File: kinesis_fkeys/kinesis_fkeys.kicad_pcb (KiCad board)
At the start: 2 copper layers, 123 x 60.5 mm, 40 parts, among them J1 RIGHT_13_TOP, J2 LEFT_13_TOP, J3 Conn_01x06, J4 Conn_01x06

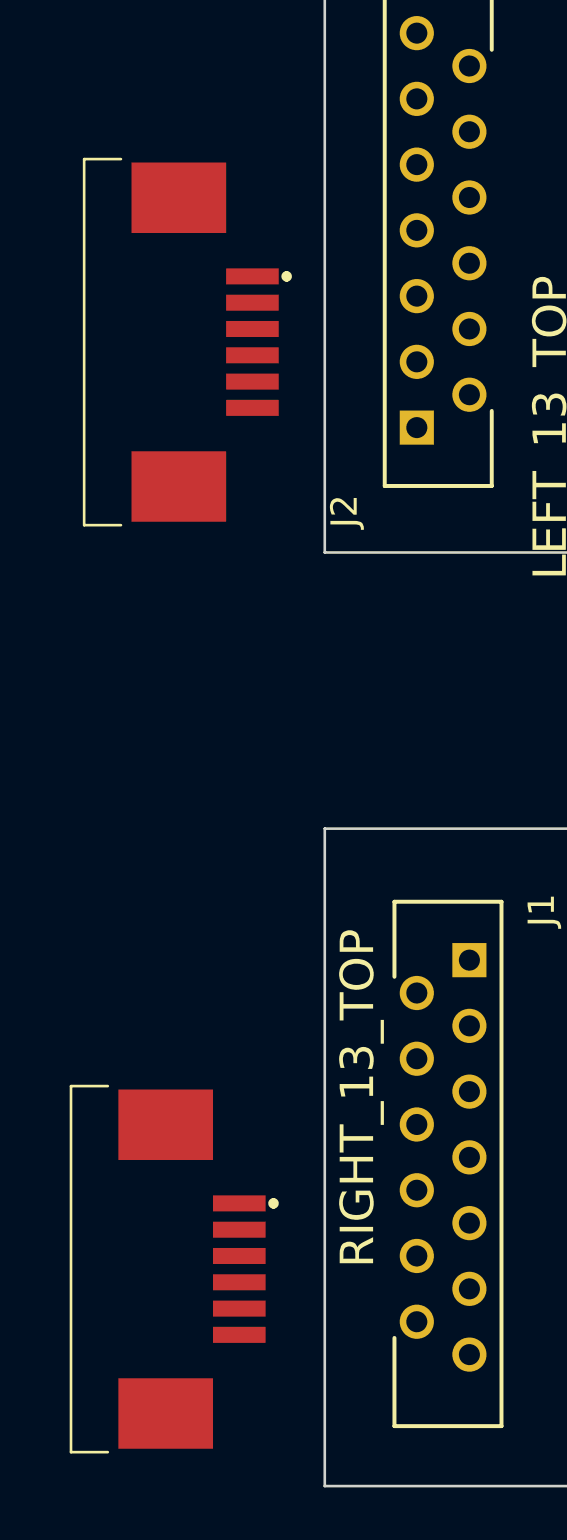
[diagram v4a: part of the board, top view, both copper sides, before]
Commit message: fixed wrong amount pins on the footprint and sorted pinout on the connectors
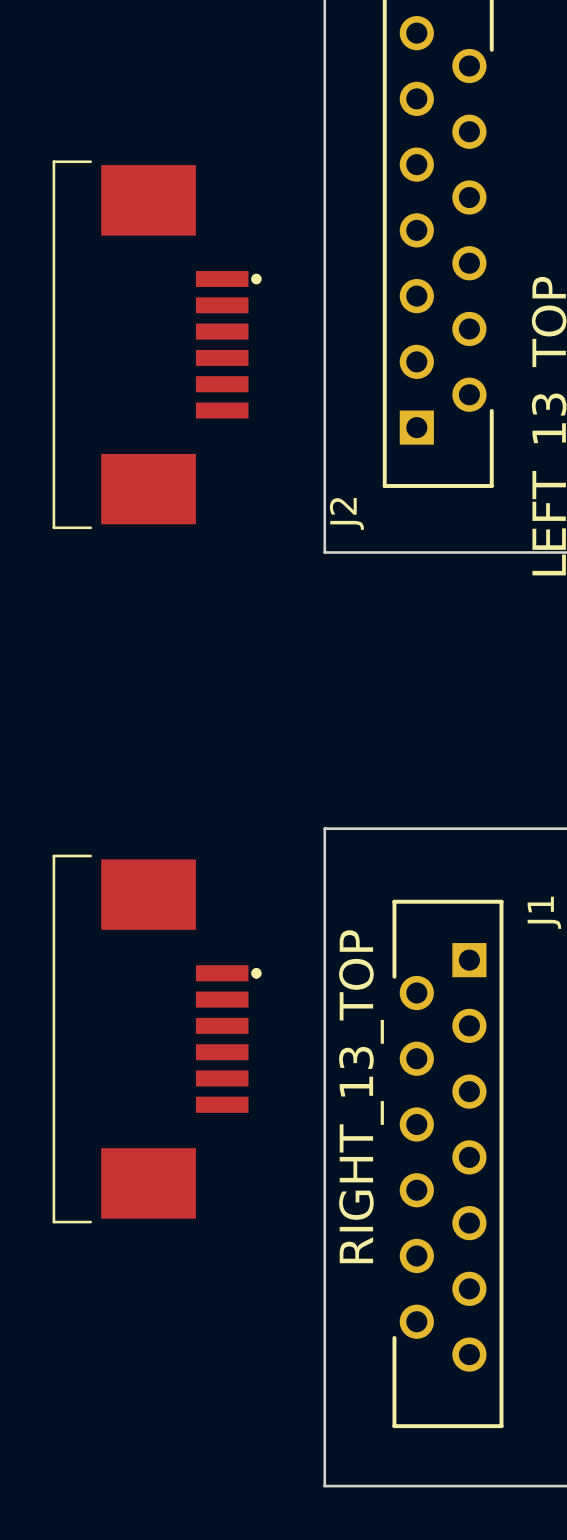
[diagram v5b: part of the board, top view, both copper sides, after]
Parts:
- removed J4: Conn_01x06, dodo_conn:84953-6
- added J5: Conn_01x08, dodo_conn:84953-6, F.Cu at (79.3, 80.2)
- J3: value Conn_01x06 -> Conn_01x08
- moved J3 8.77 mm to (79.3, 106.6)
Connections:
- J3 pad 1: /right_fkeys/COL_5 -> /right_fkeys/ROW_ESC
- J3 pad 2: /right_fkeys/COL_3 -> /right_fkeys/ROW_F1
- J3 pad 3: /right_fkeys/COL_4 -> /right_fkeys/ROW_F2
- J3 pad 4: /right_fkeys/ROW_F2 -> /right_fkeys/COL_3
- J3 pad 5: /right_fkeys/ROW_F1 -> /right_fkeys/COL_4
- J3 pad 6: /right_fkeys/ROW_ESC -> /right_fkeys/COL_5
- J3 pad 7: (no net) -> GND
- J3 pad 8: (no net) -> GND

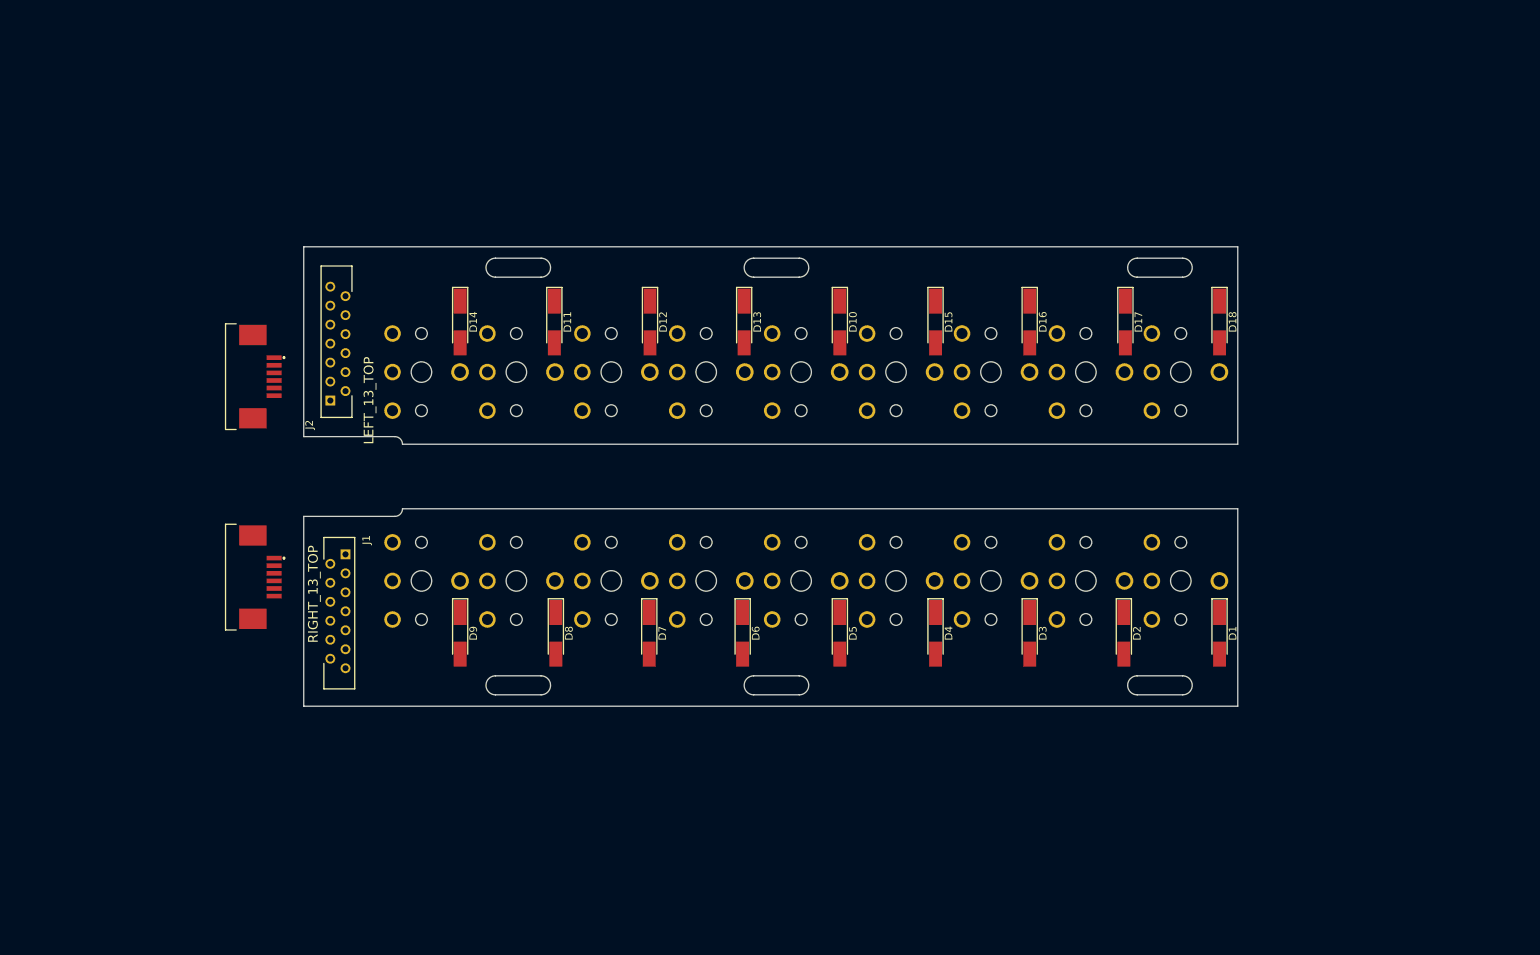
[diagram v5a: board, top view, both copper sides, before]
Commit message: positioning of components and added filled zones
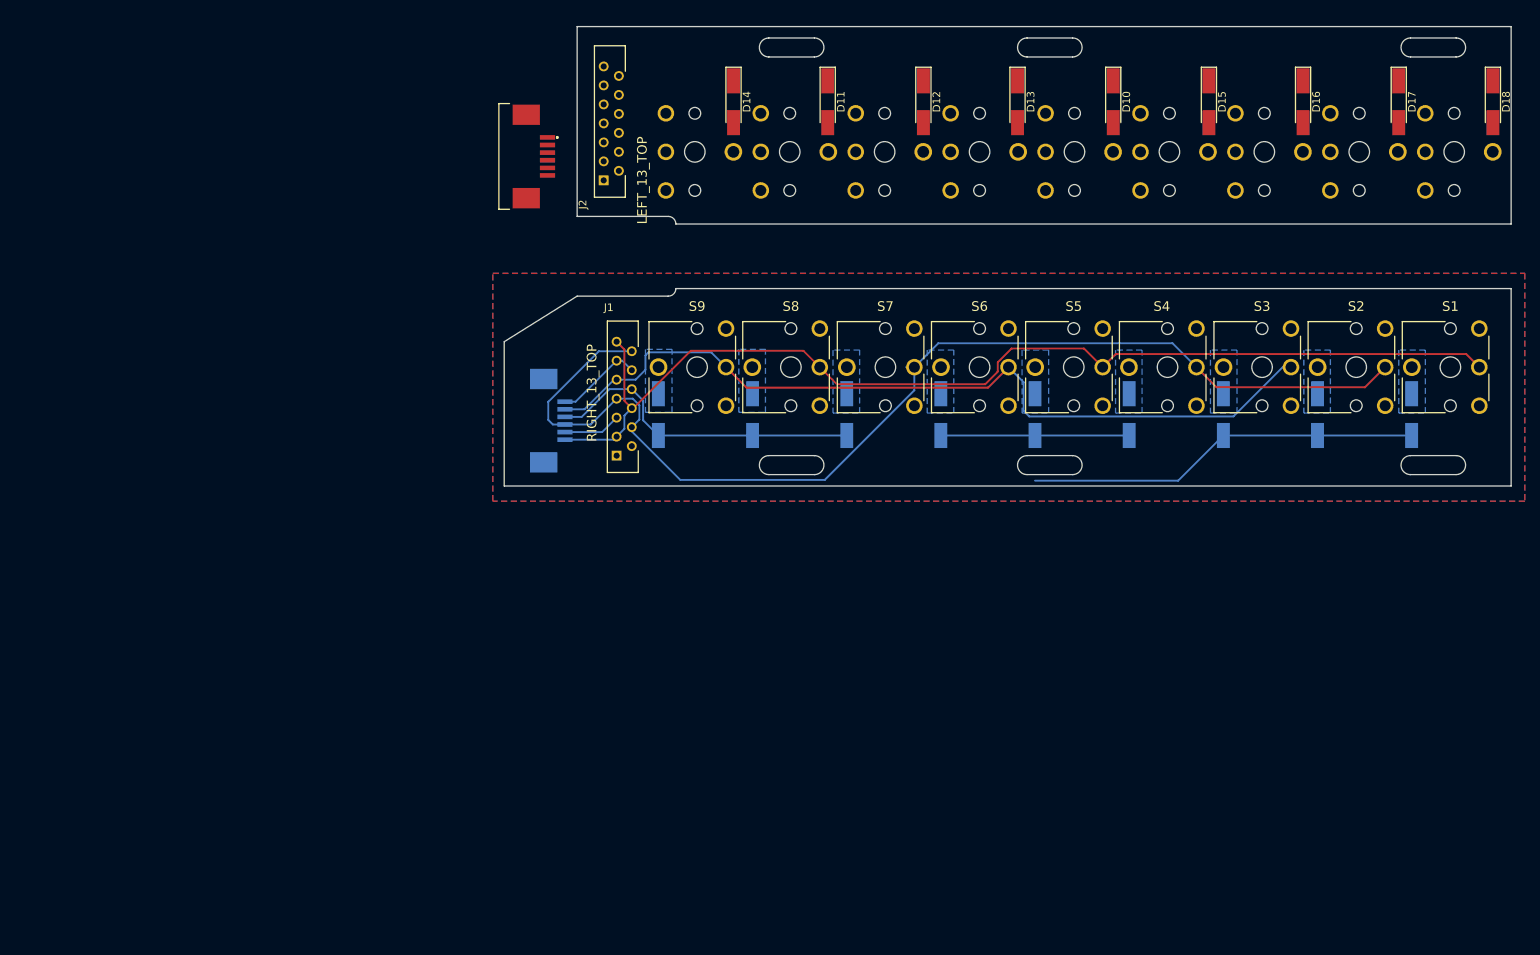
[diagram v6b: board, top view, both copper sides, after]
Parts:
- D1, D2, D3, D4, D5, D6, D7, D8, D9, J3: moved to B.Cu
- S1, S2, S3, S4, S5, S6, S7, S8, S9: moved to F.Cu
- moved S9 52.2 mm to (141.3, 73.9)
- moved S8 52.0 mm to (153.7, 73.9)
- moved S7 52.0 mm to (166.1, 73.9)
- moved S6 51.9 mm to (178.5, 73.9)
- moved S5 51.8 mm to (190.9, 73.9)
- moved S4 51.7 mm to (203.3, 73.9)
- moved S3 51.7 mm to (215.7, 73.9)
- moved S2 51.6 mm to (228.1, 73.9)
- moved S1 51.5 mm to (240.5, 73.9)
- moved S10 46.2 mm to (233.4, 45.5)
- moved S14 46.2 mm to (170.9, 45.5)
- moved S15 46.2 mm to (183.4, 45.5)
- moved S16 46.2 mm to (195.9, 45.5)
- moved D10 46.2 mm to (192.3, 44.0)
- moved D11 46.2 mm to (154.7, 44.0)
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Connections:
- J3 pad 1: /right_fkeys/ROW_ESC -> /right_fkeys/ROW_F1
- J3 pad 2: /right_fkeys/ROW_F1 -> /right_fkeys/COL_4
- J3 pad 5: /right_fkeys/COL_4 -> /right_fkeys/ROW_ESC
- J3 pad 7: GND -> GND_R
- J3 pad 8: GND -> GND_R
- J5 pad 7: GND -> GND_L
- J5 pad 8: GND -> GND_L
- S1 pad 1: GND -> GND_R
- S1 pad 3: GND -> GND_R
- S10 pad 1: GND -> GND_L
- S10 pad 3: GND -> GND_L
- S11 pad 1: GND -> GND_L
- S11 pad 3: GND -> GND_L
- S13 pad 1: GND -> GND_L
- S13 pad 3: GND -> GND_L
- S14 pad 1: GND -> GND_L
- S14 pad 3: GND -> GND_L
- S15 pad 1: GND -> GND_L
- S15 pad 3: GND -> GND_L
- S16 pad 1: GND -> GND_L
- S16 pad 3: GND -> GND_L
- S17 pad 1: GND -> GND_L
- S17 pad 3: GND -> GND_L
- S18 pad 1: GND -> GND_L
- S18 pad 3: GND -> GND_L
- S2 pad 1: GND -> GND_R
- S2 pad 3: GND -> GND_R
- S3 pad 1: GND -> GND_R
- S3 pad 3: GND -> GND_R
- S4 pad 1: GND -> GND_R
- S4 pad 3: GND -> GND_R
- S5 pad 1: GND -> GND_R
- S5 pad 3: GND -> GND_R
- S6 pad 1: GND -> GND_R
- S6 pad 3: GND -> GND_R
- S7 pad 1: GND -> GND_R
- S7 pad 3: GND -> GND_R
- S8 pad 1: GND -> GND_R
- S8 pad 3: GND -> GND_R
- S9 pad 1: GND -> GND_R
- S9 pad 3: GND -> GND_R
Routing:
- net /right_fkeys/ROW_F2: track 0.00 -> 149.7 mm
- net /right_fkeys/ROW_F1: track 0.00 -> 142.8 mm
- net /right_fkeys/ROW_ESC: track 0.00 -> 110.5 mm
- net /right_fkeys/COL_5: track 0.00 -> 63.6 mm
- net /right_fkeys/COL_3: track 0.00 -> 42.7 mm
- net /right_fkeys/COL_4: track 0.00 -> 32.4 mm
- added copper zone on B.Cu, net GND_R
- added copper zone on F.Cu, net GND_R
- added copper zone on B.Cu, net Net-(D1-K)
- added copper zone on B.Cu, net Net-(D2-K)
- added copper zone on B.Cu, net Net-(D3-K)
- added copper zone on B.Cu, net Net-(D4-K)
- added copper zone on B.Cu, net Net-(D5-K)
- added copper zone on B.Cu, net Net-(D6-K)
- added copper zone on B.Cu, net Net-(D7-K)
- added copper zone on B.Cu, net Net-(D8-K)
- added copper zone on B.Cu, net Net-(D9-K)
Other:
- board size 123 x 60.5 mm -> 132.6 x 60.5 mm

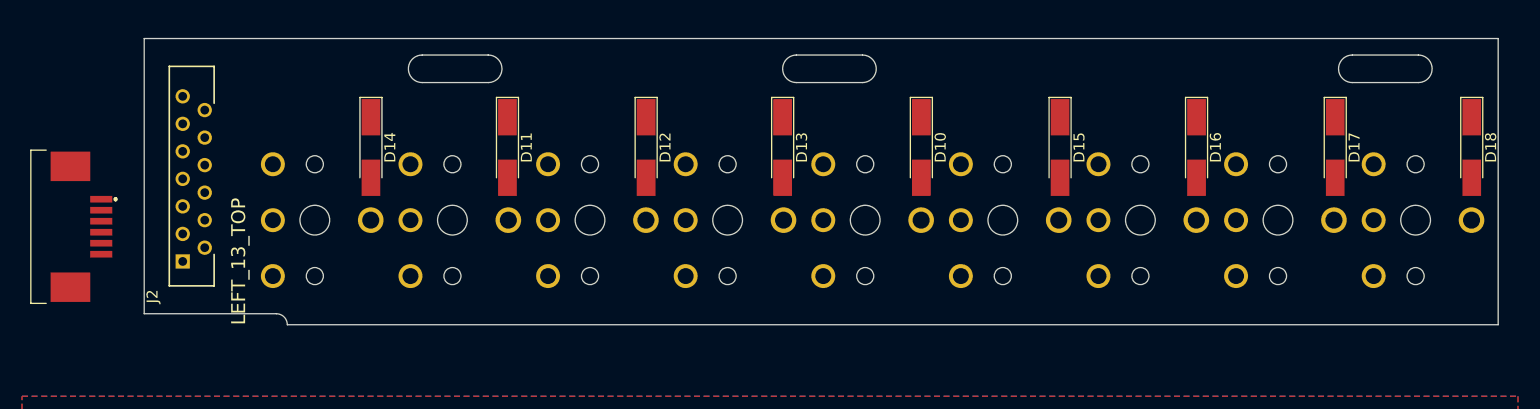
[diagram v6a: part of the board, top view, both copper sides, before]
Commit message: possitioned componentst on the pcb left
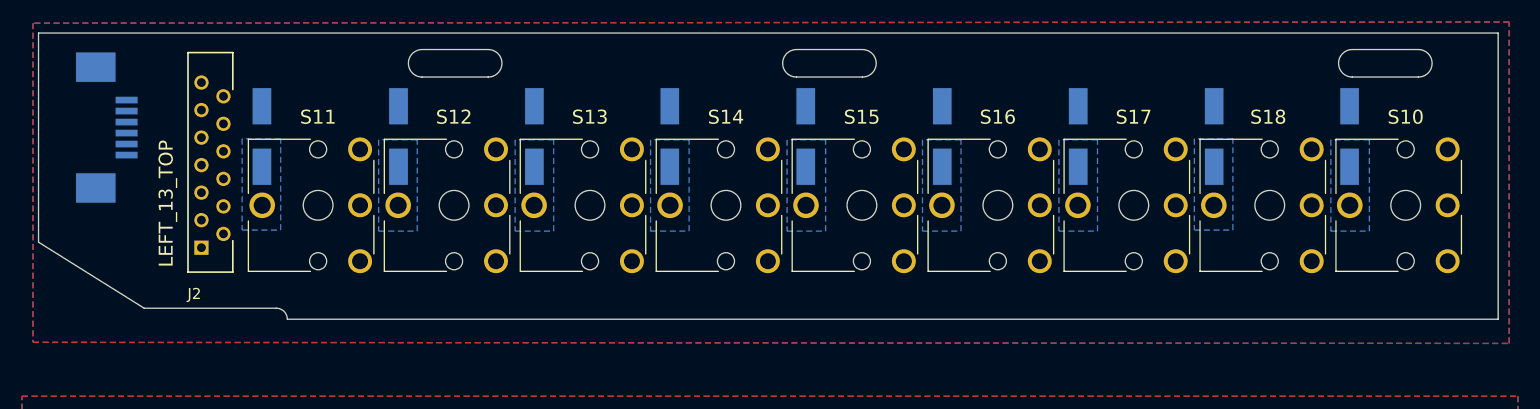
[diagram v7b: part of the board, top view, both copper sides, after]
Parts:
- D10, D11, D12, D13, D14, D15, D16, D17, D18, J5: moved to B.Cu
- S10, S11, S12, S13, S14, S15, S16, S17, S18: moved to F.Cu
- moved D18 11.1 mm to (231.2, 43.0)
- moved D17 11.0 mm to (218.9, 43.0)
- moved D16 10.8 mm to (206.5, 43.0)
- moved D15 10.7 mm to (194.2, 43.0)
- moved D10 10.5 mm to (181.8, 43.0)
- moved D13 10.3 mm to (169.4, 43.0)
- moved D12 10.2 mm to (157.1, 43.0)
- moved D11 9.95 mm to (144.8, 43.0)
- moved D14 9.95 mm to (132.4, 43.0)
- moved J5 9.30 mm to (117.6, 42.2), turned to 90 degrees
- moved S11 8.03 mm to (141.3, 44.2)
- moved S12 7.89 mm to (153.7, 44.2)
- moved S13 7.74 mm to (166.0, 44.2)
- moved S14 7.59 mm to (178.4, 44.2)
- moved S15 7.44 mm to (190.7, 44.2)
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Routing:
- added copper zone on B.Cu, net Net-(D10-A)
- added copper zone on B.Cu, net Net-(D11-A)
- added copper zone on B.Cu, net Net-(D12-A)
- added copper zone on B.Cu, net Net-(D13-A)
- added copper zone on B.Cu, net Net-(D14-A)
- added copper zone on B.Cu, net Net-(D15-A)
- added copper zone on B.Cu, net Net-(D16-A)
- added copper zone on B.Cu, net Net-(D17-A)
- added copper zone on B.Cu, net Net-(D18-A)
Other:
- board size 132.6 x 60.5 mm -> 132.6 x 61 mm
